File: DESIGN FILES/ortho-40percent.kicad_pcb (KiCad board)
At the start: 2 copper layers, 229 x 81 mm, 131 parts, among them J1 USB-C_Receptacle-24, M1 M_StencilGuide, M2 M_StencilGuide, SW1 SW_NO_4-Pin, SW10 CherryMX, SW11 CherryMX, SW12 CherryMX, SW13 CherryMX, SW14 CherryMX, SW15 CherryMX, SW16 CherryMX, SW17 CherryMX, SW18 CherryMX, SW19 CherryMX, SW2 CherryMX, SW20 CherryMX, SW21 CherryMX, SW22 CherryMX, SW23 CherryMX, SW24 CherryMX, SW25 CherryMX, SW26 CherryMX, SW27 CherryMX, SW28 CherryMX, SW29 CherryMX, SW3 CherryMX, SW30 CherryMX, SW31 CherryMX, SW32 CherryMX, SW33 CherryMX, SW34 CherryMX, SW35 CherryMX, SW36 CherryMX, SW37 CherryMX, SW38 CherryMX, SW39 CherryMX, SW4 CherryMX, SW40 CherryMX, SW41 CherryMX, SW42 CherryMX, SW43 CherryMX, SW44 CherryMX, SW45 CherryMX, SW46 CherryMX, SW47 CherryMX, SW48 CherryMX, SW49 CherryMX, SW5 CherryMX, SW50 CherryMX, SW51 CherryMX, SW6 CherryMX, SW7 CherryMX, SW8 CherryMX, SW9 CherryMX, U1 U_TPD4E05U06DQAR, U2 U_ATmega32u4-MU, Y1 XTAL_4Lead

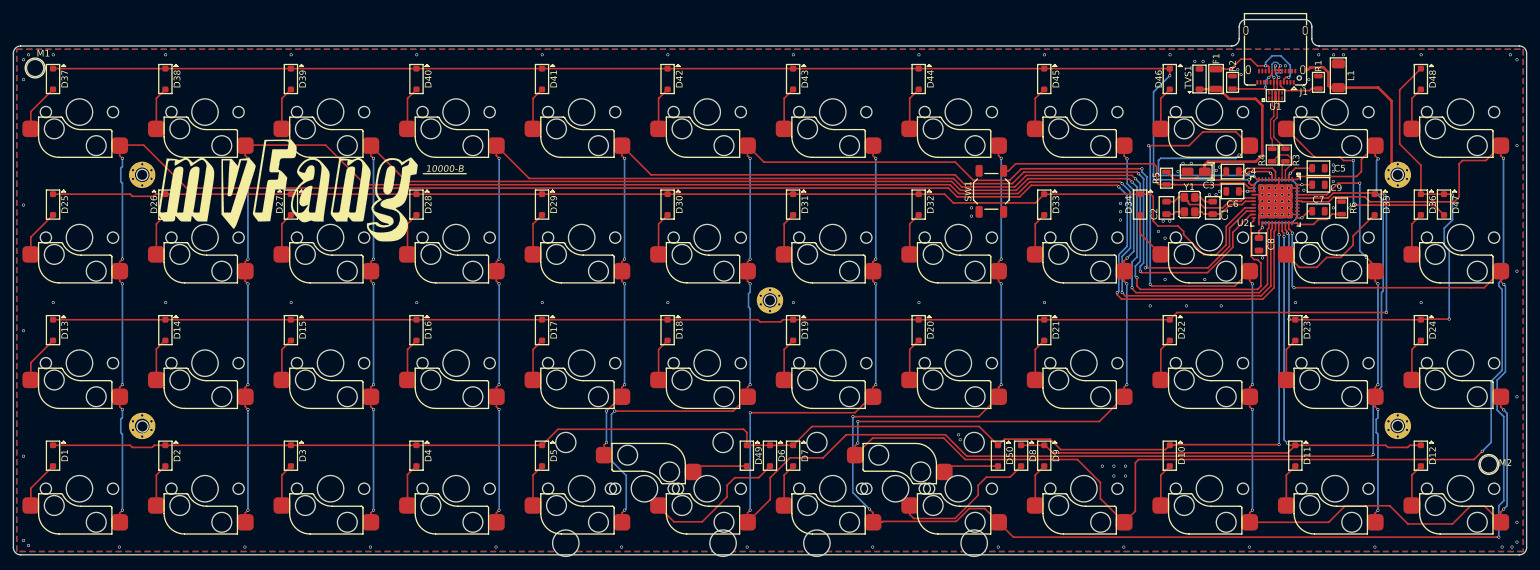
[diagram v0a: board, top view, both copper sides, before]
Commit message: Added .gitignore
Stops tracking backups and auto generated KiCad files
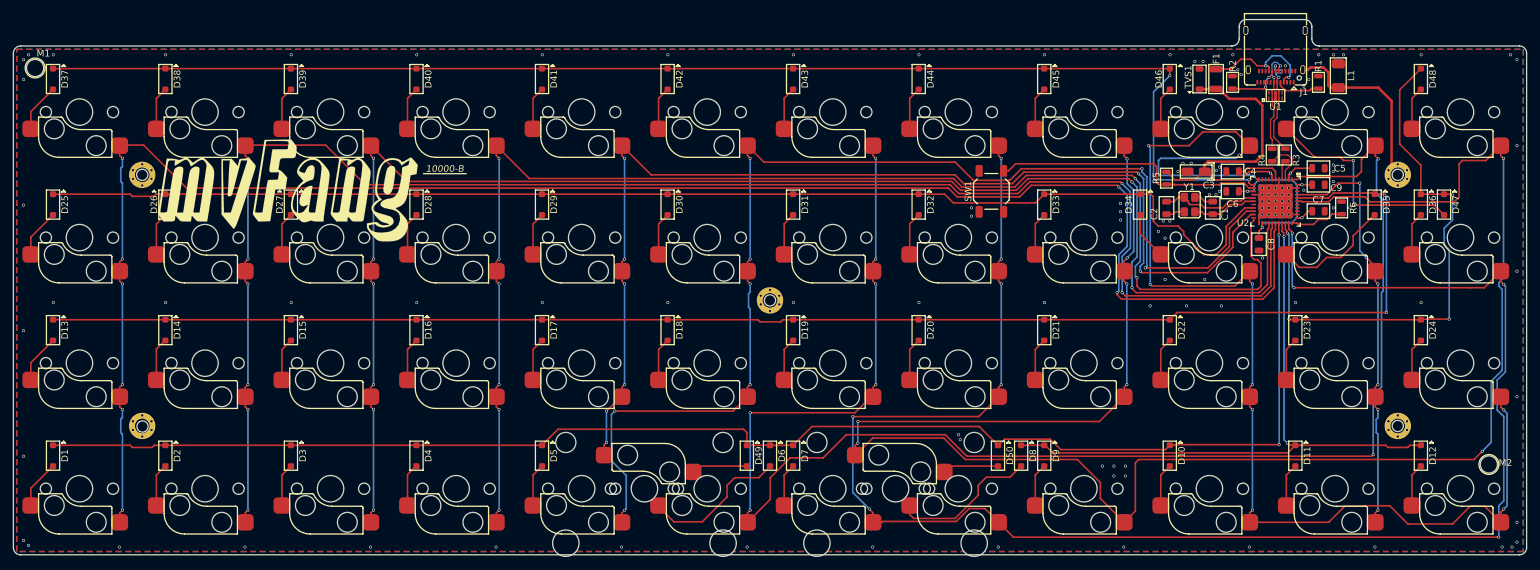
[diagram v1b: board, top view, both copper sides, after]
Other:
- outline, holes or cut-outs redrawn
- net class Default removed
- net class USB_diffPair removed
